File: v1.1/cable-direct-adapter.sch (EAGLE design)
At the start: 19 parts, among them J2 SSM-120-L-DV

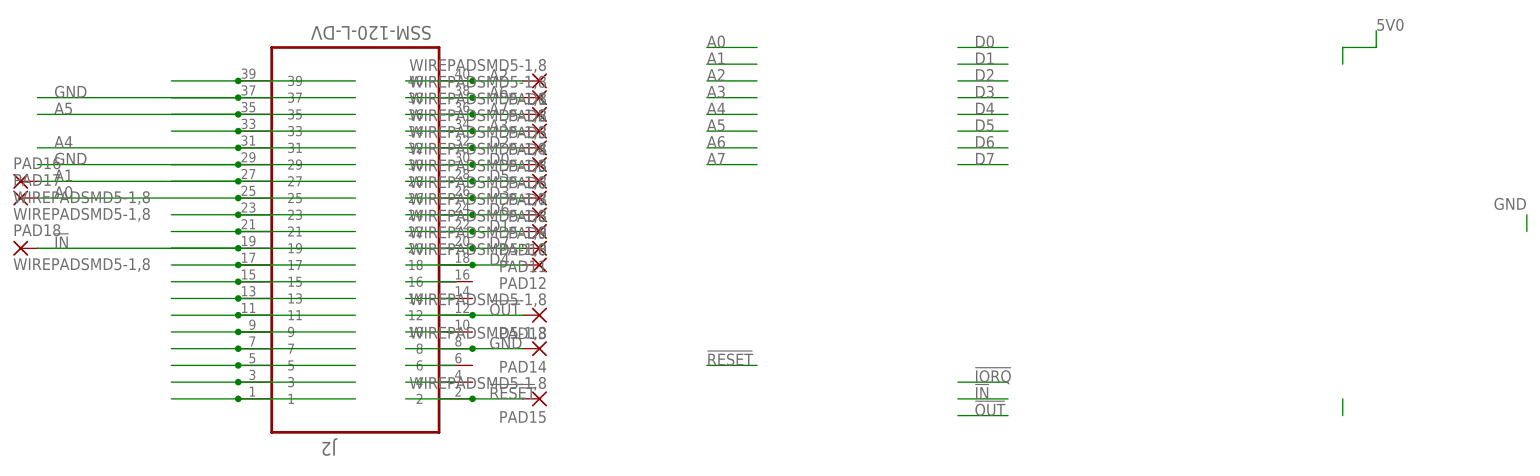
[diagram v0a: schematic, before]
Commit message: add xilinx code and finish direct adapter
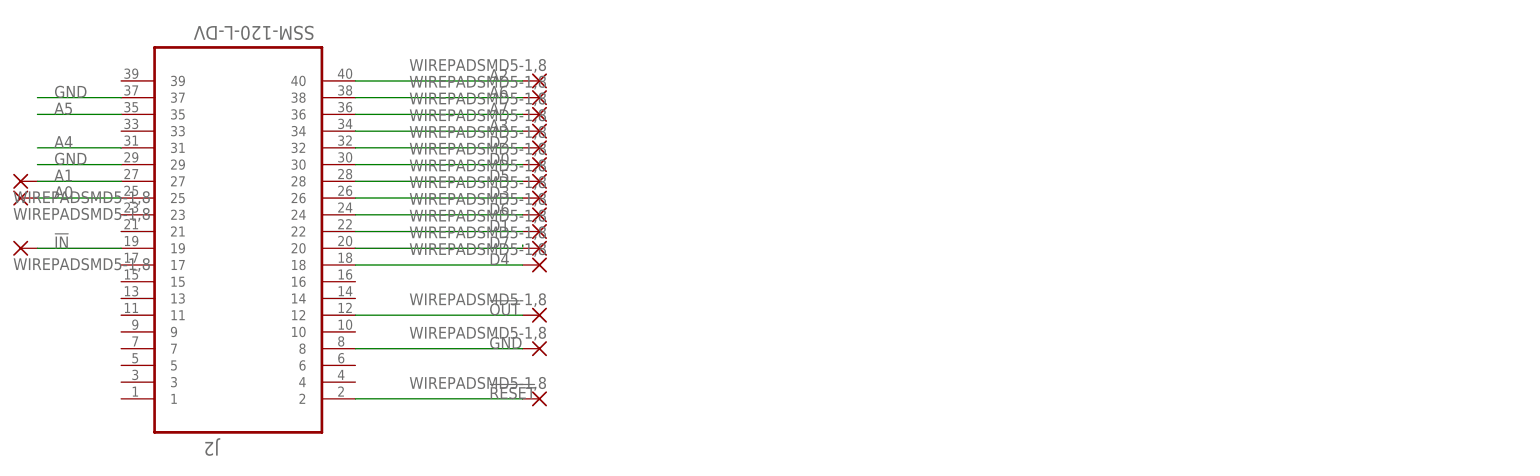
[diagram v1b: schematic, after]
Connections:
- removed net N$1: J2.1
- removed net N$10: J2.17
- removed net N$11: J2.21
- removed net N$12: J2.23
- removed net N$13: J2.33
- removed net N$14: J2.39
- removed net N$2: J2.3
- removed net N$3: J2.5
- removed net N$5: J2.7
- removed net N$6: J2.9
- removed net N$7: J2.11
- removed net N$8: J2.13
- removed net N$9: J2.15
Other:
- moved on the sheet: J2
